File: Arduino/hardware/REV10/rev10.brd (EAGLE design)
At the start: 68.6 x 53.3 mm, 28 parts, among them IC1 ATmega328P-PU, Q1 32768Hz, U1 TC1185SMD, U2 ARDUINOR3-DIMENSION

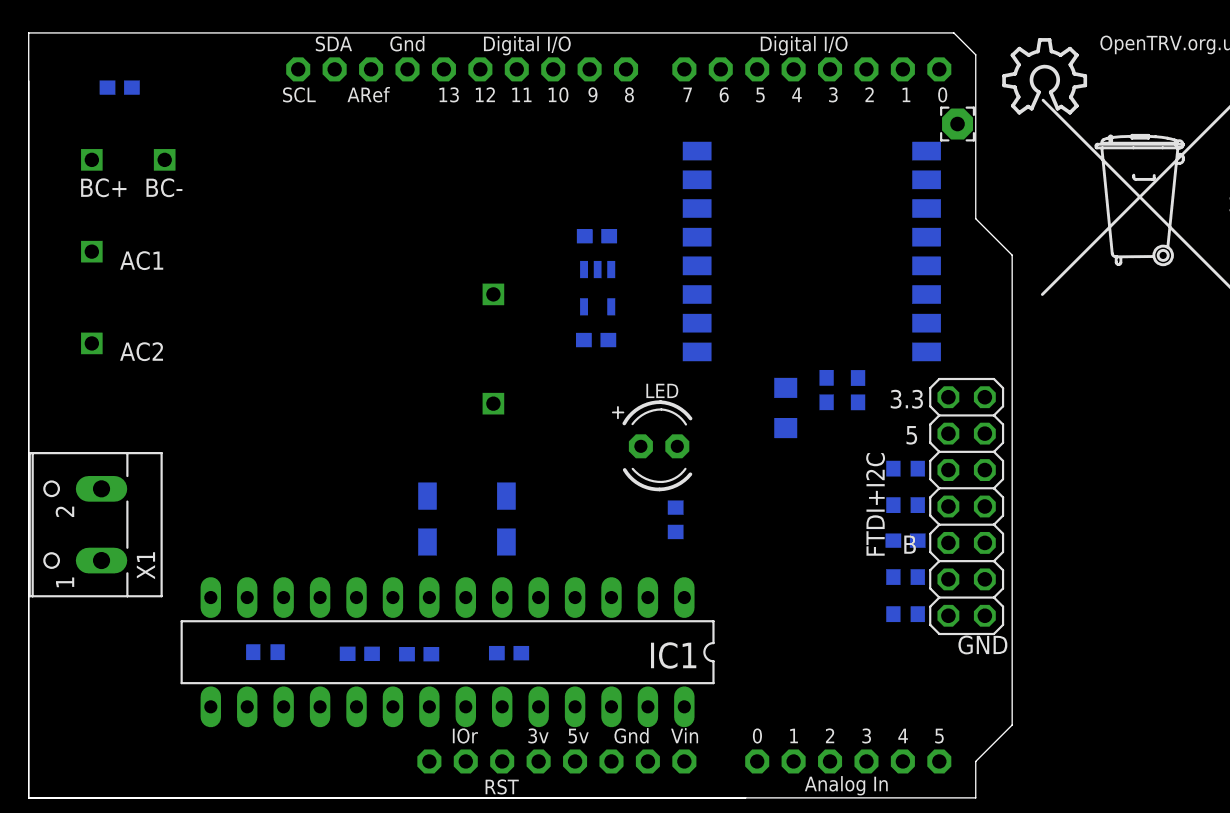
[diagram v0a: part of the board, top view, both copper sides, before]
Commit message: updated rev10 to smd avr and placed i2c connector
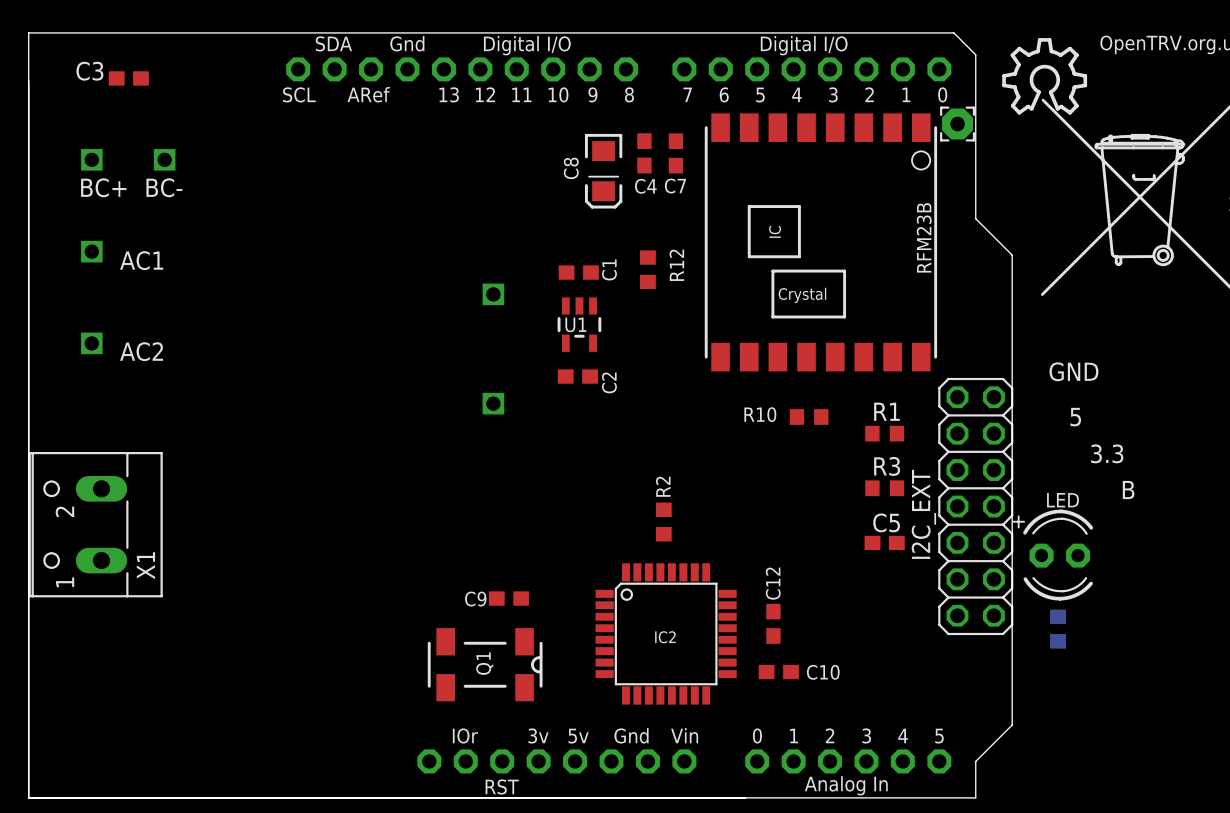
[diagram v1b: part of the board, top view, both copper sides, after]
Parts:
- removed C11: 100nF, resistor:C0603
- removed FTDI+I2C: (no value), pinhead:2X07
- removed IC1: ATmega328P-PU, Arduino-AVR:DIL28-3
- removed R4, R5: 4.7K, resistor:R0603
- added C5: 100nF, resistor:C0603
- added I2C_EXT: (no value), pinhead:2X07
- added IC2: ATMEGA168-AU, Arduino-AVR:TQFP32-08
- added R1, R3: 4.7K, resistor:R0603
- moved R12 37.7 mm to (43.2, 36.8), flipped to the top, turned to 270 degrees
- moved C10 29.2 mm to (52.3, 8.78), flipped to the top
- moved LED 29.0 mm to (71.9, 16.9)
- moved R7 27.7 mm to (71.8, 11.8)
- moved C12 24.8 mm to (51.9, 12.1), flipped to the top, turned to 90 degrees
- moved C7 20.8 mm to (45.1, 44.9), flipped to the top
- moved C4 20.8 mm to (42.9, 44.9), flipped to the top
- moved C8 20.8 mm to (40.1, 43.7), flipped to the top
- moved R2 17.3 mm to (44.3, 19.2), flipped to the top, turned to 270 degrees
- moved R10 15.3 mm to (54.4, 26.6), flipped to the top, turned to 180 degrees
- moved Q1 10.2 mm to (31.8, 9.28), flipped to the top
- moved C9 3.81 mm to (33.5, 13.9), flipped to the top
- moved C1 2.84 mm to (38.4, 36.6), flipped to the top
- moved C2 2.84 mm to (38.3, 29.4), flipped to the top
- moved U1 2.84 mm to (38.4, 33.0), flipped to the top
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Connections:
- removed net N$1: C11.2, FTDI+I2C.11
- removed net N$3: FTDI+I2C.7, R5.2
- removed net N$5: FTDI+I2C.9, R4.2
- new net D2: I2C_EXT.14
- new net N$25: C5.2, I2C_EXT.5
- new net N$26: I2C_EXT.12, R3.2
- new net N$28: I2C_EXT.11, R1.2
- net 5V: no longer FTDI+I2C.12
- net BOILER: now also IC2.10; no longer FTDI+I2C.6, IC1.12
- net GND: now also I2C_EXT.6, IC2.21, IC2.3, IC2.5; no longer FTDI+I2C.1, FTDI+I2C.3, IC1.22, IC1.8
- net LED_HEATCALL_L: now also IC2.2; no longer IC1.6
- net N$14: now also IC2.23; no longer IC1.23
- net N$15: now also IC2.24; no longer IC1.24
- net N$16: now also IC2.25; no longer IC1.25
- net N$17: now also IC2.26; no longer IC1.26
- net N$19: now also IC2.12; no longer IC1.14
- net N$20: now also IC2.9; no longer IC1.11
- net N$21: now also IC2.11; no longer IC1.13
- net N$22: now also IC2.32; no longer IC1.4
- net N$24: now also IC2.1; no longer IC1.5
- net N$6: now also IC2.20; no longer IC1.21
- net RESET: now also C5.1, IC2.29; no longer C11.1, IC1.1
- net RFM_IRQ: now also I2C_EXT.7, IC2.13; no longer IC1.15
- net RX: now also IC2.31, R1.1; no longer IC1.3, R4.1
- net SCL: now also I2C_EXT.9, IC2.28; no longer FTDI+I2C.2, IC1.28
- net SDA: now also I2C_EXT.10, IC2.27; no longer FTDI+I2C.4, IC1.27
- net SPI_MISO: now also I2C_EXT.1, IC2.16; no longer IC1.18
- net SPI_MOSI: now also I2C_EXT.4, IC2.15; no longer IC1.17
- net SPI_NSS: now also I2C_EXT.8, IC2.14; no longer IC1.16
- net SPI_SCK: now also I2C_EXT.3, IC2.17; no longer IC1.19
- net TX: now also IC2.30, R3.1; no longer IC1.2, R5.1
- net VCC: now also I2C_EXT.2, IC2.18, IC2.4, IC2.6; no longer FTDI+I2C.14, IC1.20, IC1.7
- net XTAL1: now also IC2.7, Q1.1; no longer IC1.9, Q1.4
- net XTAL2: now also IC2.8, Q1.4; no longer IC1.10, Q1.1

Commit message: updates to rev10 as per deniz spec
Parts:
- added R4: 4.7K, resistor:R0603
- added R5: 330R, resistor:R0603
- moved U$1 66.6 mm to (18.5, 3.33)
- moved LED 57.3 mm to (14.8, 13.1)
- moved U$2 53.7 mm to (24.0, 32.8)
- moved R7 51.8 mm to (20.0, 13.4), flipped to the top, turned to 0 degrees
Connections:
- new net N$1: IC2.11, R4.1
- new net N$3: IC2.12, R5.1
- net N$19: now also R5.2; no longer IC2.12
- net N$21: now also R4.2; no longer IC2.11
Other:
- board text removed: "3.3"
- board text removed: "5"
- board text removed: "B"
- board text removed: "GND"
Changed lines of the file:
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@@
 <?xml version="1.0" encoding="utf-8"?>
 <!DOCTYPE eagle SYSTEM "eagle.dtd">
-<eagle version="7.3.0">
+<eagle version="7.4.0">
 <drawing>
 <settings>
@@
 <wire x1="0" y1="0" x2="50" y2="0" width="0" layer="20"/>
 <wire x1="0" y1="50" x2="0" y2="0" width="0" layer="20"/>
-<text x="89.931028125" y="41.91376875" size="1" layer="25" font="vector" ratio="10" rot="R180">20140910</text>
-<text x="69.830803125" y="34.704378125" size="1" layer="22" font="vector" ratio="10" rot="MR180">License: http://goo.gl/3d71UJ</text>
-<text x="74.661121875" y="52.14046875" size="1" layer="25" font="vector" ratio="10">OpenTRV.org.uk</text>
-<text x="76.1413" y="20.8341625" size="1.27" layer="25" font="vector" rot="SR0">B</text>
-<text x="73.963396875" y="23.354459375" size="1.27" layer="25" font="vector" rot="SR0">3.3</text>
-<text x="71.094565625" y="29.078415625" size="1.27" layer="25" font="vector" rot="SR0">GND</text>
-<text x="72.521103125" y="25.9296625" size="1.27" layer="25" font="vector" ratio="10" rot="SR0">5</text>
+<text x="11.191028125" y="1.27376875" size="1" layer="25" font="vector" ratio="10" rot="R180">20140910</text>
+<text x="10.140803125" y="46.134378125" size="1" layer="22" font="vector" ratio="10" rot="MR180">License: http://goo.gl/3d71UJ</text>
+<text x="1.83453125" y="0.366121875" size="1" layer="25" font="vector" ratio="10" rot="R90">OpenTRV.org.uk</text>
 <text x="12.7" y="26.67" size="0.8128" layer="26" rot="MR90">Seal of solderpads with
  hotmelt glue or silicone
@@
 <attribute name="NAME" x="42.21066875" y="42.1472375" size="1" layer="25" font="vector" ratio="10"/>
 </element>
-<element name="R7" library="resistor" package="R0603" value="470R" x="71.78678125" y="11.771834375" smashed="yes" rot="MR90">
-<attribute name="NAME" x="69.68328125" y="11.138834375" size="1" layer="26" font="vector" ratio="10" rot="MR90"/>
+<element name="R7" library="resistor" package="R0603" value="470R" x="19.978165625" y="13.36678125" smashed="yes">
+<attribute name="NAME" x="19.345165625" y="11.26328125" size="1" layer="25" font="vector" ratio="10"/>
 </element>
 <element name="C1" library="resistor" package="C0603" value="10uF 10V" x="38.357740625" y="36.628115625" smashed="yes">
@@
 <attribute name="NAME" x="39.00734375" y="33.491321875" size="1" layer="25" font="vector" ratio="10" rot="R180"/>
 </element>
-<element name="U$2" library="logo" package="TONNE" value="" x="77.335" y="39.15211875"/>
+<element name="U$2" library="logo" package="TONNE" value="" x="23.995" y="32.80211875"/>
 <element name="R2" library="resistor" package="R0603" value="4.7K" x="44.288953125" y="19.2370875" smashed="yes" rot="R270">
 <attribute name="NAME" x="44.7578" y="20.87400625" size="1" layer="25" font="vector" ratio="10" rot="R90"/>
@@
 <attribute name="NAME" x="54.19625" y="8.2561" size="1" layer="25" font="vector" ratio="10"/>
 </element>
-<element name="U$1" library="ohw-logo" package="OSHW_10X200_NOTEXT" value="" x="68.014165625" y="47.77610625"/>
+<element name="U$1" library="ohw-logo" package="OSHW_10X200_NOTEXT" value="" x="18.484165625" y="3.32610625"/>
 <element name="C12" library="resistor" package="C0603" value="100nF" x="51.93130625" y="12.1406125" smashed="yes" rot="R90">
 <attribute name="NAME" x="52.41930625" y="13.7516125" size="1" layer="25" font="vector" ratio="10" rot="R90"/>
@@
 <attribute name="NAME" x="49.786653125" y="26.223978125" size="1" layer="25" font="vector" ratio="10"/>
 </element>
-<element name="LED" library="adafruit" package="LED3MM" value="" x="71.9" y="16.895" smashed="yes">
-<attribute name="NAME" x="73.31055625" y="21.25808125" size="1" layer="25" font="vector" ratio="10" rot="R180"/>
-<attribute name="VALUE" x="74.44" y="14.609" size="1.27" layer="27" ratio="10"/>
+<element name="LED" library="adafruit" package="LED3MM" value="" x="14.75" y="13.085" smashed="yes">
+<attribute name="NAME" x="16.16055625" y="17.44808125" size="1" layer="25" font="vector" ratio="10" rot="R180"/>
+<attribute name="VALUE" x="17.29" y="10.799" size="1.27" layer="27" ratio="10"/>
 </element>
 <element name="RFM23B" library="SparkFun-RF" package="RFM23-XXX-S1" value="RFM23B" x="55.245" y="38.735" smashed="yes" rot="R270">
@@
 <element name="IC2" library="Arduino-AVR" package="TQFP32-08" value="ATMEGA168-AU" x="44.45" y="11.43" smashed="yes">
 <attribute name="NAME" x="43.5864" y="10.795" size="0.8128" layer="25"/>
+</element>
+<element name="R4" library="resistor" package="R0603" value="4.7K" x="36.83" y="21.59" smashed="yes" rot="R90">
+<attribute name="NAME" x="35.941" y="20.701" size="1.27" layer="25" rot="R90"/>
+</element>
+<element name="R5" library="resistor" package="R0603" value="330R" x="40.64" y="21.59" smashed="yes" rot="R90">
+<attribute name="NAME" x="39.751" y="20.701" size="1.27" layer="25" rot="R90"/>
 </element>
 </elements>
@@
 <wire x1="42.939840625" y1="44.0983" x2="45.13053125" y2="44.08946875" width="0" layer="19" extent="16-16"/>
 <wire x1="40.09278125" y1="42.299175" x2="42.939840625" y2="44.0983" width="0" layer="19" extent="16-16"/>
-<wire x1="70.63" y1="16.895" x2="40.09278125" y2="42.299175" width="0" layer="19" extent="16-16"/>
-<wire x1="39.146290625" y1="29.38355625" x2="70.63" y2="16.895" width="0" layer="19" extent="16-16"/>
+<wire x1="13.48" y1="13.085" x2="40.09278125" y2="42.299175" width="0" layer="19" extent="16-16"/>
+<wire x1="39.146290625" y1="29.38355625" x2="13.48" y2="13.085" width="0" layer="19" extent="16-16"/>
 <wire x1="39.355234375" y1="31.70184375" x2="39.146290625" y2="29.38355625" width="0" layer="19" extent="16-16"/>
 <wire x1="44.288953125" y1="20.0870875" x2="45.13053125" y2="44.08946875" width="0" layer="19" extent="16-16"/>
-<wire x1="34.346934375" y1="13.903546875" x2="70.63" y2="16.895" width="0" layer="19" extent="16-16"/>
+<wire x1="34.346934375" y1="13.903546875" x2="13.48" y2="13.085" width="0" layer="19" extent="16-16"/>
 <wire x1="53.1543875" y1="8.77630625" x2="34.346934375" y2="13.903546875" width="0" layer="19" extent="16-16"/>
 <wire x1="43.18" y1="35.98" x2="53.1543875" y2="8.77630625" width="0" layer="19" extent="16-16"/>
@@
 <contactref element="R7" pad="1"/>
 <contactref element="IC2" pad="2"/>
-<wire x1="40.1574" y1="13.43" x2="71.78678125" y2="10.921834375" width="0" layer="19" extent="1-16"/>
+<wire x1="40.1574" y1="13.43" x2="19.128165625" y2="13.36678125" width="0" layer="19" extent="1-16"/>
 </signal>
 <signal name="RESET">
@@
 <contactref element="R7" pad="2"/>
 <contactref element="LED" pad="K"/>
-<wire x1="71.78678125" y1="12.621834375" x2="73.17" y2="16.895" width="0" layer="19" extent="16-16"/>
+<wire x1="20.828165625" y1="13.36678125" x2="16.02" y2="13.085" width="0" layer="19" extent="16-16"/>
 </signal>
 <signal name="N$31" class="2">
@@
 <signal name="N$19">
 <contactref element="U2" pad="D8"/>
-<contactref element="IC2" pad="12"/>
-<wire x1="44.05" y1="7.1374" x2="41.656" y2="50.8" width="0" layer="19" extent="1-1"/>
+<contactref element="R5" pad="2"/>
+<wire x1="40.64" y1="22.44" x2="41.656" y2="50.8" width="0" layer="19" extent="1-1"/>
 </signal>
 <signal name="N$22">
@@
 <contactref element="I2C_EXT" pad="14"/>
 </signal>
-<signal name="N$21">
-<contactref element="IC2" pad="11"/>
-</signal>
 <signal name="BOILER">
 <contactref element="IC2" pad="10"/>
 </signal>
+<signal name="N$21">
+<contactref element="R4" pad="2"/>
+</signal>
+<signal name="N$1">
+<contactref element="R4" pad="1"/>
+<contactref element="IC2" pad="11"/>
+<wire x1="36.83" y1="20.74" x2="43.25" y2="7.1374" width="0" layer="19" extent="1-1"/>
+</signal>
+<signal name="N$3">
+<contactref element="R5" pad="1"/>
+<contactref element="IC2" pad="12"/>
+<wire x1="40.64" y1="20.74" x2="44.05" y2="7.1374" width="0" layer="19" extent="1-1"/>
+</signal>
 </signals>

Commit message: updates as pr google doc
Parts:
- removed C3: 10uF 10V, resistor:C0603
- removed U$3: TUHS10, tuhs10:TUHS10
- added A6, A7: WIREPAD1,6/0,9, wirepad:1,6/0,9
- added LDR: BPX65, opto-trans-siemens:BPX65
- added R6: 100K, resistor:R0603
- added R8: 4K7, resistor:R0603
- added R9: 4.7K, resistor:R0603
- added TMP112: TMP1, TMP112_2:TMP112
- added U$4: VTX-214-010-205, VTX-214-010-205:VTX-214-010-205
- added USBPOWER: MICRO-USB-FCI-10103592, micro-usb-fci-10103592:MICRO-USB-FCI-10103592
- I2C_EXT: device pinhead:2X07 -> pinhead:2X07/90
- R4: value 4.7K -> 4K7
- moved U$1 80.0 mm to (85.8, 46.5)
- moved U$2 68.6 mm to (92.6, 34.7)
- moved R4 22.2 mm to (15.2, 16.5), flipped to the bottom, turned to 180 degrees
- moved Q1 21.3 mm to (49.1, 21.7), flipped to the bottom, turned to 90 degrees
- moved C12 17.6 mm to (35.0, 7.51), flipped to the bottom, turned to 0 degrees
- moved LED 13.9 mm to (24.3, 2.92)
- moved C7 13.0 mm to (57.8, 42.4), flipped to the bottom
- moved C4 13.0 mm to (55.6, 42.4), flipped to the bottom
- moved C8 13.0 mm to (52.8, 41.2), flipped to the bottom
- moved R12 12.3 mm to (55.2, 34.3), flipped to the bottom, turned to 0 degrees
- moved R7 6.44 mm to (26.0, 11.1), flipped to the bottom, turned to 270 degrees
- moved X1 6.25 mm to (3.81, 12.8)
- moved C2 4.07 mm to (35.8, 32.6), flipped to the bottom
- moved C1 4.07 mm to (35.8, 39.8), flipped to the bottom
- moved U1 4.07 mm to (35.9, 36.2), flipped to the bottom
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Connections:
- removed net N$11: C3.1, U$3.BC-
- removed net N$12: C3.2, U$3.BC+
- removed net N$14: IC2.23, U2.A0
- removed net N$21: R4.2
- removed net N$22: IC2.32, U2.D2
- new net 5V1: USBPOWER.1
- new net IO_POWER_UP: IC2.11, LDR.K
- new net LDR: IC2.23, LDR.A, R6.1
- new net N$5: A7.1, IC2.22
- net 5V: no longer U$3.+
- net D2: now also IC2.32, R9.1
- net GND: now also R6.2, TMP112.2, TMP112.4, USBPOWER.17, USBPOWER.5, USBPOWER.7; no longer U$3.-
- net N$1: now also A6.1, IC2.19; no longer IC2.11, R4.1
- net N$4: no longer U$3.AC2
- net N$8: now also U$4.L; no longer U$3.AC1
- net SCL: now also R8.1, TMP112.1
- net SDA: now also R4.2, TMP112.6
- net VCC: now also R4.1, R8.2, R9.2, TMP112.5

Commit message: updates as pr google doc and guidance from mark and deniz
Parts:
- removed A6, A7: WIREPAD1,6/0,9, wirepad:1,6/0,9
- added JP1: (no value), pinhead:2X04/90
- added LED1: (no value), adafruit:LED3MM
- added R11: 470R, resistor:R0603
- added R13: 1K, resistor:R0603
- added R14: 10K, resistor:R0603
- added T1: (no value), transistor:SOT23-EBC
- added X2: (no value), con-wago-500:W237-102
- moved R1 11.5 mm to (57.1, 14.0)
- moved C5 6.48 mm to (57.1, 24.1)
- moved USBPOWER 5.08 mm to (8.25, 3.70), flipped to the bottom
- moved R3 4.02 mm to (57.1, 17.8)
- moved I2C_EXT 2.84 mm to (69.8, 20.3)
- renumbered LDR to PHT, U$4 to PSU
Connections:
- removed net N$17: IC2.26, U2.A3
- removed net N$24: IC2.1, U2.D3
- new net N$11: IC2.25
- new net N$12: R13.2, R14.2, T1.B
- new net N$14: LED1.K, T1.C, X2.1
- new net VOICE: IC2.1
- net 5V: now also R11.2, X2.2
- net BOILER: now also R13.1
- net GND: now also JP1.5, R14.1, T1.E
- net N$1: now also JP1.1; no longer A6.1
- net N$16: now also LED1.A, R11.1; no longer IC2.25, U2.A2
- net N$19: no longer U2.D8
- net N$20: no longer U2.D5
- net N$5: now also JP1.3; no longer A7.1

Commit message: minor changes to board
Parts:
- removed JP1: (no value), pinhead:2X04/90
- added JP2: (no value), pinhead:2X03/90
- moved R14 76.1 mm to (34.3, 38.1), flipped to the bottom
- moved X2 72.9 mm to (2.54, 48.3), turned to 90 degrees
- moved T1 68.7 mm to (31.8, 43.2), flipped to the bottom
- moved R13 67.7 mm to (27.9, 38.1), flipped to the bottom
- moved LED1 63.2 mm to (13.3, 50.8)
- moved R11 55.7 mm to (26.7, 44.5), flipped to the bottom
- moved X1 11.5 mm to (2.54, 24.2)
- moved C4 8.89 mm to (64.5, 42.4)
- moved C5 8.89 mm to (66.0, 24.1)
- moved R1 8.89 mm to (66.0, 14.0)
- moved R12 8.89 mm to (64.1, 34.3)
- moved R3 8.89 mm to (66.0, 17.8)
- moved RFM23B 8.89 mm to (64.1, 38.7)
- moved R7 8.89 mm to (34.9, 11.1)
- moved ANT1 8.89 mm to (73.7, 47.0)
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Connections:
- net 5V: now also JP2.4, PSU.+
- net GND: now also JP2.5, PSU.-; no longer JP1.5
- net N$1: now also JP2.1; no longer JP1.1
- net N$4: now also PSU.N
- net N$5: now also JP2.3; no longer JP1.3
- net VCC: now also JP2.6
- net VOICE: now also JP2.2

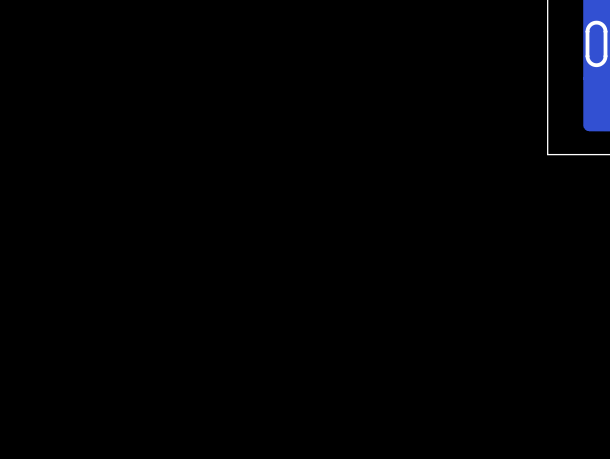
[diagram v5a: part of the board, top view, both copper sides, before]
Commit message: pfet placed
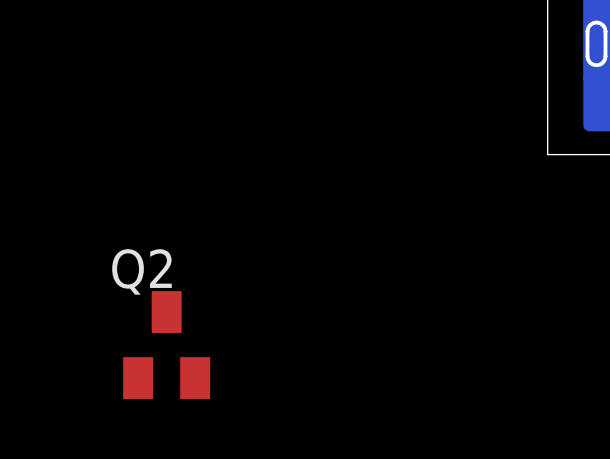
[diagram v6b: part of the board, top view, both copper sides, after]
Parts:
- added Q2: BSS84, transistor-small-signal:SOT23
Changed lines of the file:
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@@
 <attribute name="VALUE" x="3.81" y="42.545" size="1.27" layer="27" rot="R180"/>
 </element>
+<element name="Q2" library="transistor-small-signal" package="SOT23" value="BSS84" x="-3.81" y="-6.35"/>
 </elements>
 <signals>
